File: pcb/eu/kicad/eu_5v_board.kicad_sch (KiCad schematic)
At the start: 6 parts, among them J1 Socket 1x2 2.54, P1 P70-2200045 GND, P2 P70-2200045 +5V

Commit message: Parts: replace the obsolete Murata capacitors, gold SSW socket on the EU 5 V board
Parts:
- C1: MPN GRM31CR61A226KE19L -> CL31A226KPHNNNE; Manufacturer Murata -> Samsung Electro-Mechanics
- J1: MPN SSW-102-01-L-S -> SSW-102-01-G-S
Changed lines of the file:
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@@
 			)
 		)
-		(property "MPN" "SSW-102-01-L-S"
+		(property "MPN" "SSW-102-01-G-S"
 			(at 35.56 91.44 0)
 			(effects
@@
 			)
 		)
-		(property "Datasheet" "https://www.murata.com"
-			(at 76.2 91.44 0)
-			(effects
-				(font
-					(size 1.27 1.27)
-				)
-				(hide yes)
-			)
-		)
-		(property "Description" "Ceramic 22 uF 10 V X5R 1206 (or equivalent)"
-			(at 76.2 91.44 0)
-			(effects
-				(font
-					(size 1.27 1.27)
-				)
-				(hide yes)
-			)
-		)
-		(property "Manufacturer" "Murata"
-			(at 76.2 91.44 0)
-			(effects
-				(font
-					(size 1.27 1.27)
-				)
-				(hide yes)
-			)
-		)
-		(property "MPN" "GRM31CR61A226KE19L"
-			(at 76.2 91.44 0)
-			(effects
+		(property "Datasheet" "https://www.samsungsem.com"
+			(at 76.2 91.44 0)
+			(effects
+				(font
+					(size 1.27 1.27)
+				)
+				(hide yes)
+			)
+		)
+		(property "Description" "Ceramic 22 uF 10 V X5R 1206, 1.8 mm max (or equivalent)"
+			(at 76.2 91.44 0)
+			(effects
+				(font
+					(size 1.27 1.27)
+				)
+				(hide yes)
+			)
+		)
+		(property "Manufacturer" "Samsung Electro-Mechanics"
+			(at 76.2 91.44 0)
+			(effects
+				(font
+					(size 1.27 1.27)
+				)
+				(hide yes)
+			)
+		)
+		(property "MPN" "CL31A226KPHNNNE"
+			(at 76.2 91.44 0)
+			(effects

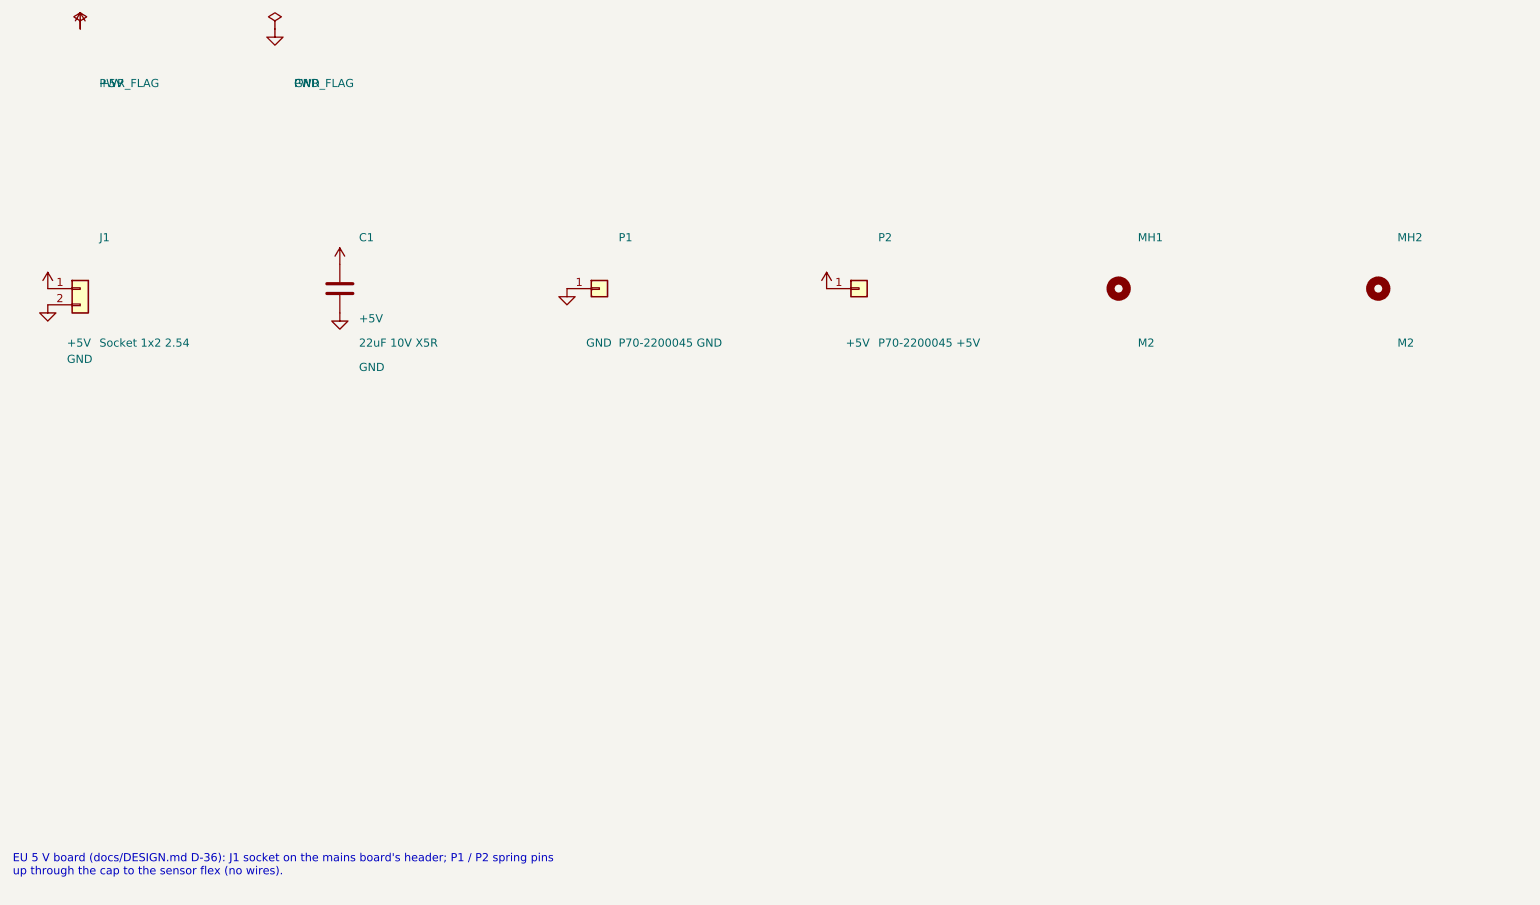
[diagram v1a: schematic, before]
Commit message: Boards for v0.4: ring board, mic carrier, riser, cover flex, EU cap board, wiring board posts
- Ring board, mic carrier and riser in pcb/sensor/ (D-50, D-60, D-68); carrier and riser fab
  packs; the ring board waits on the MSR-2's CN2 part and map
- Riser 14 x 12 mm, pins above and between the posts; cover flex with the run past the GND
  contact post and a jog from the pad section (D-79)
- EU cap board on the carrier, closed snap windows, wider with the face plate (D-56, D-70,
  D-77, D-78); EU 5 V board pins follow the back cover's pads
- Wiring board: WA-SMSI spacer posts in the 5 V area (SMT, spigot inside the board), J2
- ERC / DRC clean on every board
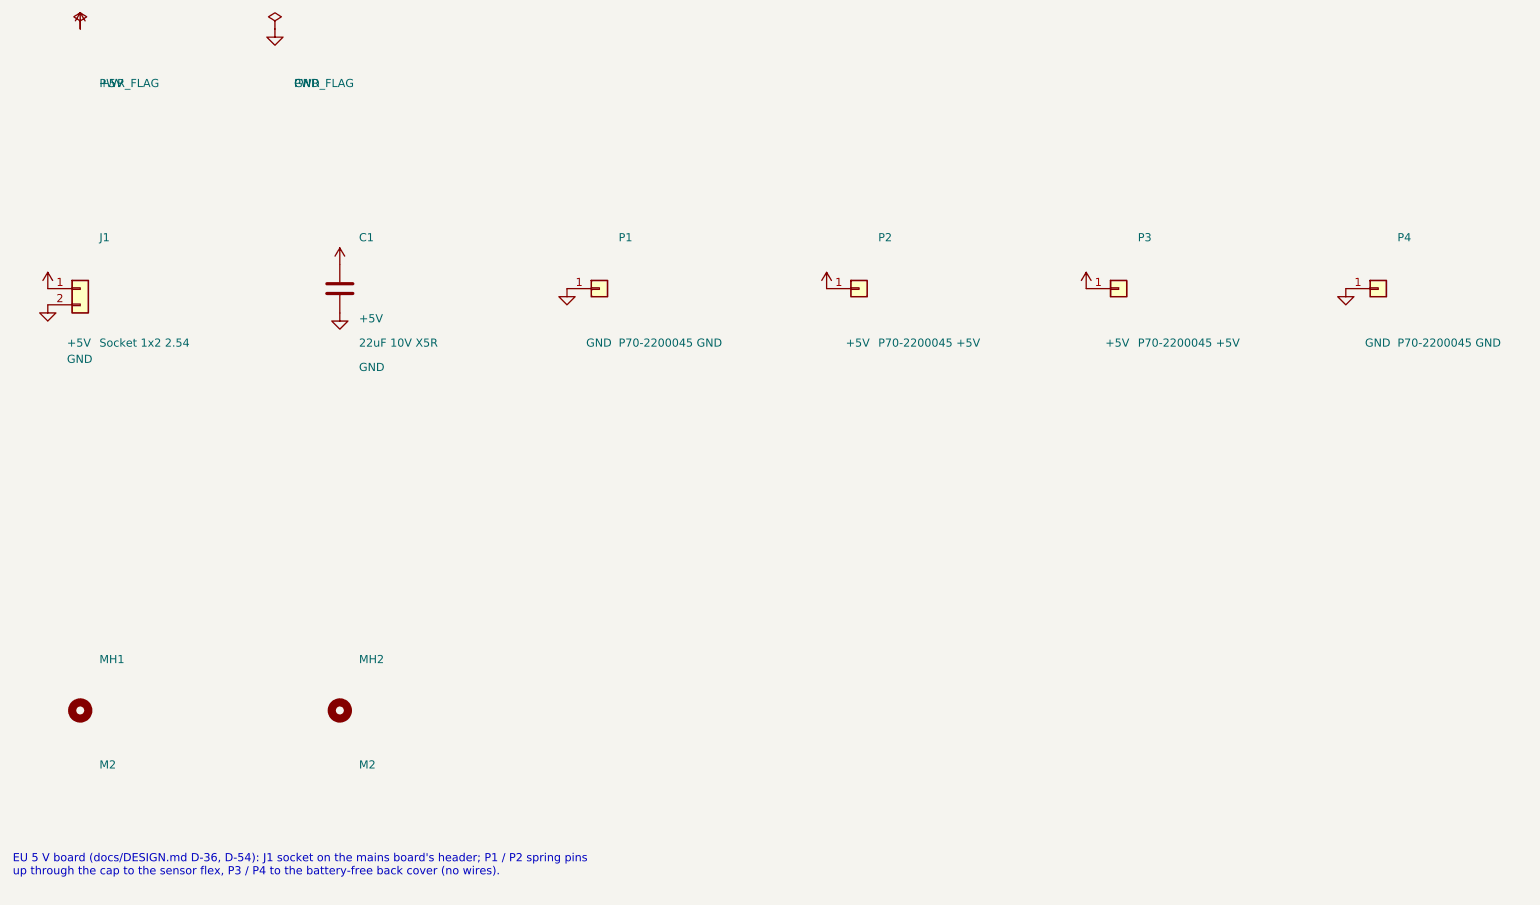
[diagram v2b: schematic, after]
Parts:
- added P3: P70-2200045 +5V, eu:Harwin_P70-2200045, symbol eu:Conn_01x01
- added P4: P70-2200045 GND, eu:Harwin_P70-2200045, symbol eu:Conn_01x01
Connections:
- net +5V: now also P3.1 (Pin_1)
- net GND: now also P4.1 (Pin_1)
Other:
- note added: "EU 5 V board (docs/DESIGN.md D-36, D-54): J1 socket on the mains board's header; P1 / P2 spring pins up through the cap to the sensor flex, P3 / P4 to the battery-free back cover (no wires)."
- note removed: "EU 5 V board (docs/DESIGN.md D-36): J1 socket on the mains board's header; P1 / P2 spring pins up through the cap to the sensor flex (no wires)."
- moved on the sheet: MH1, MH2

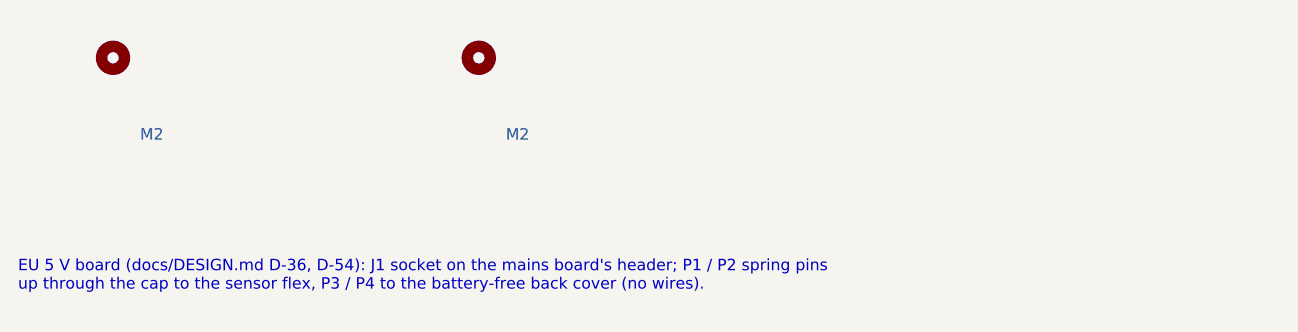
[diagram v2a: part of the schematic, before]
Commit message: Board generators: shared P70 and WA-SMSI footprints, fixed revision date, EU boards v0.4
- One Harwin P70 footprint with its 3D model for the riser and the EU 5 V board; one
  WA-SMSI land pattern for the wiring board posts and the ring board spacers
- Shared library-table and symbol helpers; dead code from removed boards gone
- REV_DATE replaces today's date on silkscreen and title blocks
- EU boards v0.4; EU cap board fab pack written once CN2 is confirmed
- Order lists key the EU header as TSM-102-02-L-SV (D-59)
- ERC / DRC clean on every board
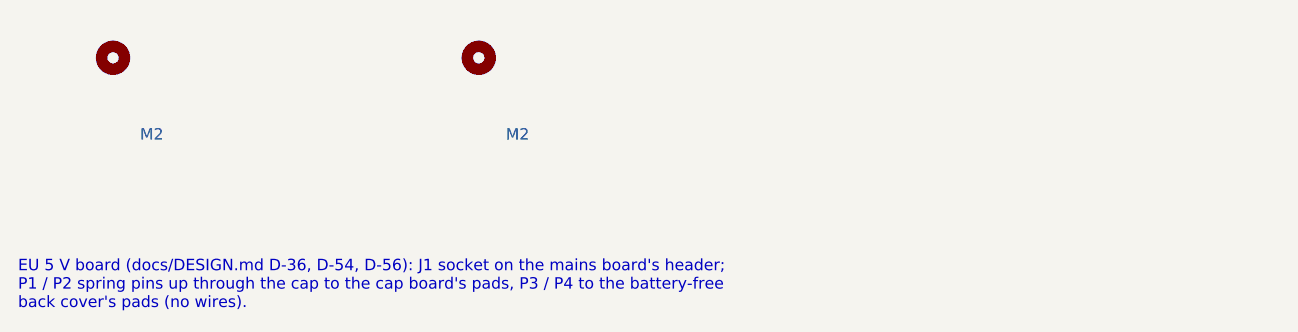
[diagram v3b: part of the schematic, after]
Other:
- note added: "EU 5 V board (docs/DESIGN.md D-36, D-54, D-56): J1 socket on the mains board's header; P1 / P2 spring pins up through the cap to the cap board's pads, P3 / P4 to the battery-free back cover's pads (no wires)."
- note removed: "EU 5 V board (docs/DESIGN.md D-36, D-54): J1 socket on the mains board's header; P1 / P2 spring pins up through the cap to the sensor flex, P3 / P4 to the battery-free back cover (no wires)."
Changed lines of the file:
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@@
 		(title "Smart wall plate - EU 5 V board")
 		(date "2026-10-11")
-		(rev "v0.2")
+		(rev "v0.4")
 		(company "smart-wallplate")
 		(comment 1 "Generated by pcb/eu/tools/gen_eu.py - edit eu_parts.py")
@@
 		)
 	)
-	(text "EU 5 V board (docs/DESIGN.md D-36, D-54): J1 socket on the mains board's header; P1 / P2 spring pins\nup through the cap to the sensor flex, P3 / P4 to the battery-free back cover (no wires)."
+	(text "EU 5 V board (docs/DESIGN.md D-36, D-54, D-56): J1 socket on the mains board's header;\nP1 / P2 spring pins up through the cap to the cap board's pads, P3 / P4 to the battery-free\nback cover's pads (no wires)."
 		(exclude_from_sim no)
 		(at 25 180 0)

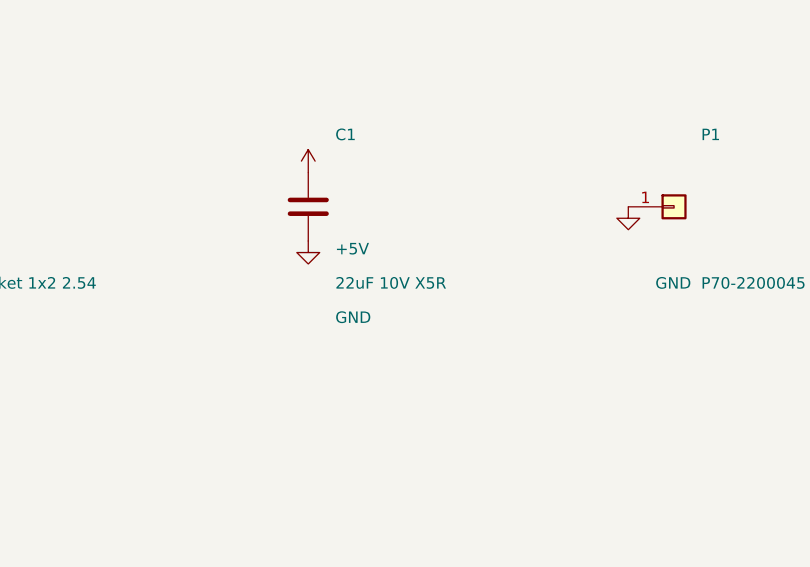
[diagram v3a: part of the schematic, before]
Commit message: Parts and order lists: EU PE connector, 22 uF C1, unit and devkit lists, E-Switch rocker (D-94, D-95, D-97)
- D-94: the EU lights' PE joined in the box in a WAGO 221-412 (EXTRA_EU, ASSEMBLY step 5); the
  boards carry no PE; the steel piece's insulation added to the EU review checklist
- D-95: 22 uF C1 KEMET C1206C226M4PACTU (16 V X5R, 1.8 max) on the ring board, the EU cap board
  and the EU 5 V board; the Samsung CL31A226KPHNNNE has a 61-week maker lead time
- D-97: make order writes unit_na, unit_eu, devkit_na, devkit_eu (4 sets per variant,
  DEVKIT_SETS), exact counts; the PCBWay packs are the devkit (5 PCBs per design); the old
  3 NA + 2 EU lists removed
- Rocker: both variants' lists take the E-Switch RA412C1100 (RA4 datasheet rating option C:
  UL/cUL 10 A 250 VAC; ENEC 10(4) A 250 V~); the Marquardt stays the reference part
- ADAU7002 to DigiKey in Mouser orders (Mouser does not restock it); stale PCBWay notes fixed
- Boards ERC / DRC clean; renders regenerated
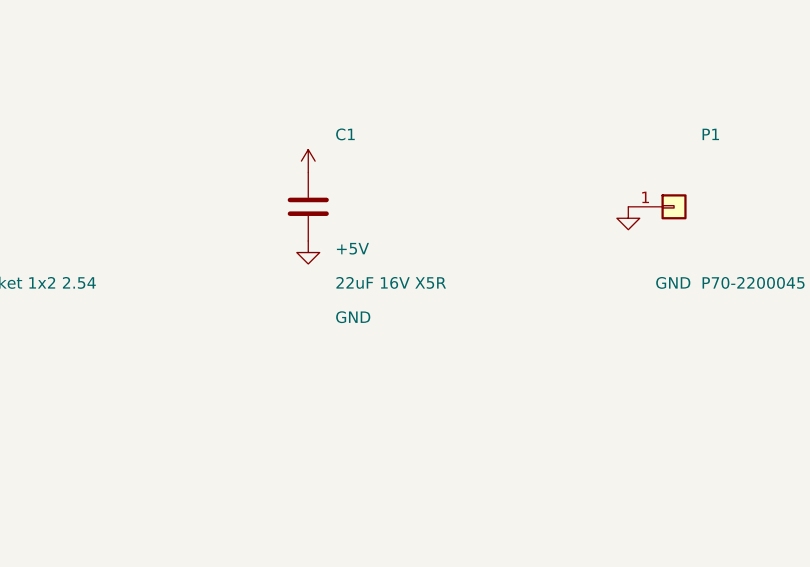
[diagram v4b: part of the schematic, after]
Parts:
- C1: value 22uF 10V X5R -> 22uF 16V X5R; MPN CL31A226KPHNNNE -> C1206C226M4PACTU; Manufacturer Samsung Electro-Mechanics -> KEMET
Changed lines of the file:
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@@
 			)
 		)
-		(property "Value" "22uF 10V X5R"
+		(property "Value" "22uF 16V X5R"
 			(at 79.2 99.94 0)
 			(effects
@@
 			)
 		)
-		(property "Datasheet" "https://www.samsungsem.com"
+		(property "Datasheet" "https://yageogroup.com/content/datasheet/asset/file/KEM_C1006_X5R_SMD"
 			(at 76.2 91.44 0)
 			(effects
@@
 			)
 		)
-		(property "Description" "Ceramic 22 uF 10 V X5R 1206, 1.8 mm max (or equivalent)"
+		(property "Description" "Ceramic 22 uF 16 V X5R 1206, 1.8 mm max"
 			(at 76.2 91.44 0)
 			(effects
@@
 			)
 		)
-		(property "Manufacturer" "Samsung Electro-Mechanics"
+		(property "Manufacturer" "KEMET"
 			(at 76.2 91.44 0)
 			(effects
@@
 			)
 		)
-		(property "MPN" "CL31A226KPHNNNE"
+		(property "MPN" "C1206C226M4PACTU"
 			(at 76.2 91.44 0)
 			(effects

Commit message: Flex review fixes, back cover clip, README, Sladdseg, order lists (D-116..D-119)
- D-116: cover flex: 0603 X5R input/output caps, ESD diode TPD1E10B06DYAR,
  0.6 mm bend radius with relief slits, stiffener notch and outlines,
  coverlay expansion, mask-defined pin pads, teardrops, fab notes; the
  cover's snap hooks allow for stiffener adhesive and tolerance
- D-117, D-118: bottom clip catch 3.22 above the floor, tip as far proud of
  the shell as the top clip's
- Battery polarity confirmed on a unit
- README rewritten: three editions, assembly renders, safety and polarity
  warnings, cost for 1 to 10,000 plates, printed parts; detail and board
  renders moved to their docs; the product is named Sladdseg
- EU boards: the ant logo on the other face
- D-119: order lists: one NA plate, one EU plate, a devkit of 5 + 5
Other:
- title: Smart wall plate - EU 5 V board -> Sladdseg - EU 5 V board
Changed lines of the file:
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@@
 	(paper "A4")
 	(title_block
-		(title "Smart wall plate - EU 5 V board")
+		(title "Sladdseg - EU 5 V board")
 		(date "2026-10-12")
 		(rev "v0.5")
